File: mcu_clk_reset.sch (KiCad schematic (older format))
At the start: 52 parts, among them J4 20021121-00010C4LF, J5 M20-8762042, Q3 BSS214NW, Q4 BSS214NW, Q5 BSS214NW, Q6 BSS214NW, U4 IS25WP032D, U5 FE310-G002, X1 KX2132709Z, Y1 TSX-3225 16.0000MF18X-AC0

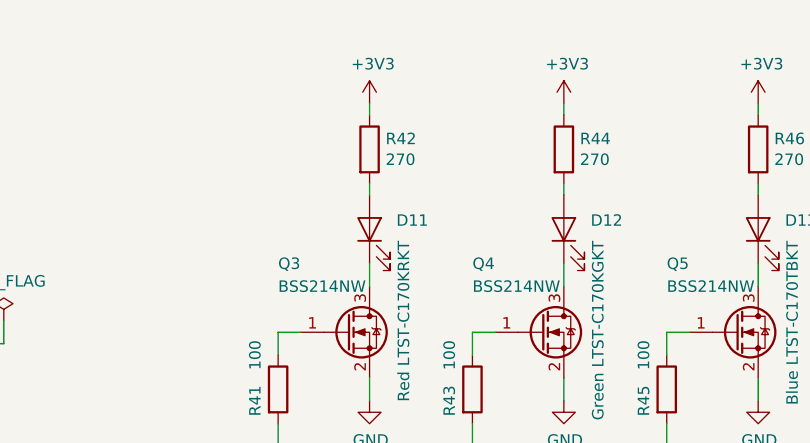
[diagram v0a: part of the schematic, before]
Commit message: Change resistor values to adjust LED brightness
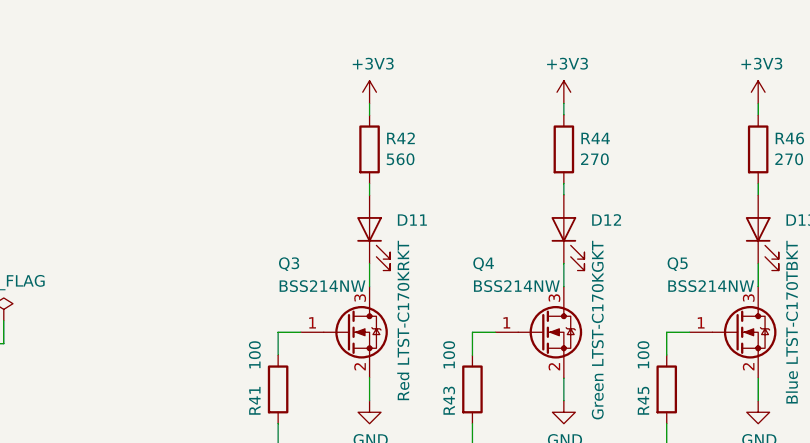
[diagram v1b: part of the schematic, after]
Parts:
- R42: value 270 -> 560
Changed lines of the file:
@@
 AR Path="/5E14DB51/5EBB9395" Ref="R42"  Part="1"
 F 0 "R42" H 8170 1196 50  0000 L CNN
-F 1 "270" H 8170 1105 50  0000 L CNN
+F 1 "560" H 8170 1105 50  0000 L CNN
 F 2 "Resistor_SMD:R_0603_1608Metric_Pad1.05x0.95mm_HandSolder" V 8030 1150 50  0001 C CNN
 F 3 "~" H 8100 1150 50  0001 C CNN

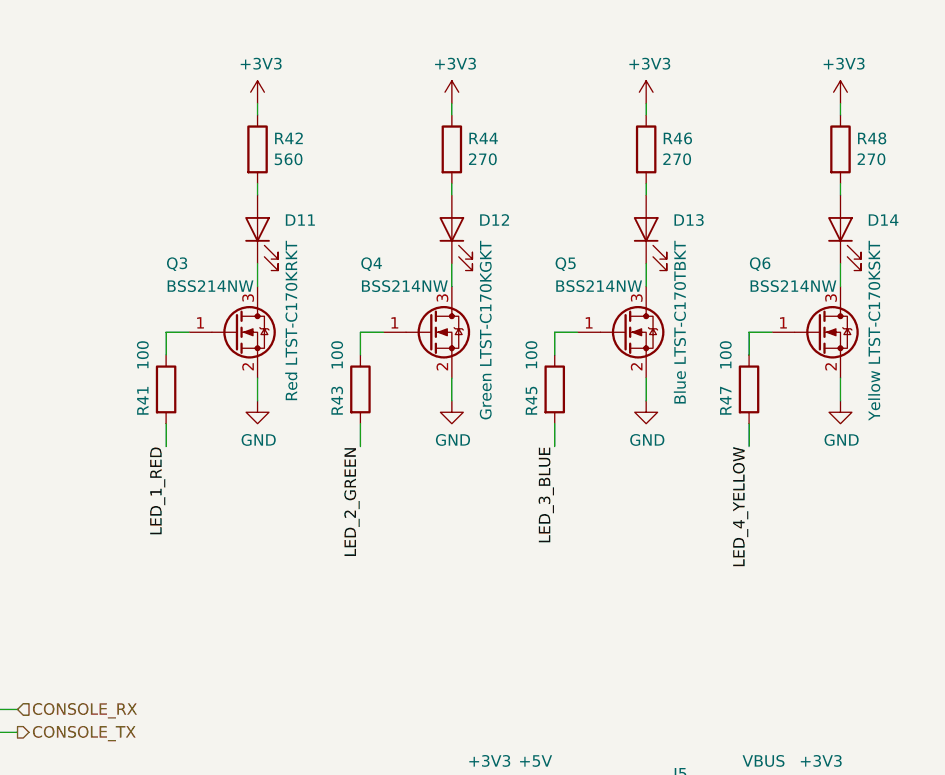
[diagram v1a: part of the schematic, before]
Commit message: Add 10k pull-downs on MCU LED outputs, improve layout
Pushed few traces, fixed DRC issue on one of the vias.
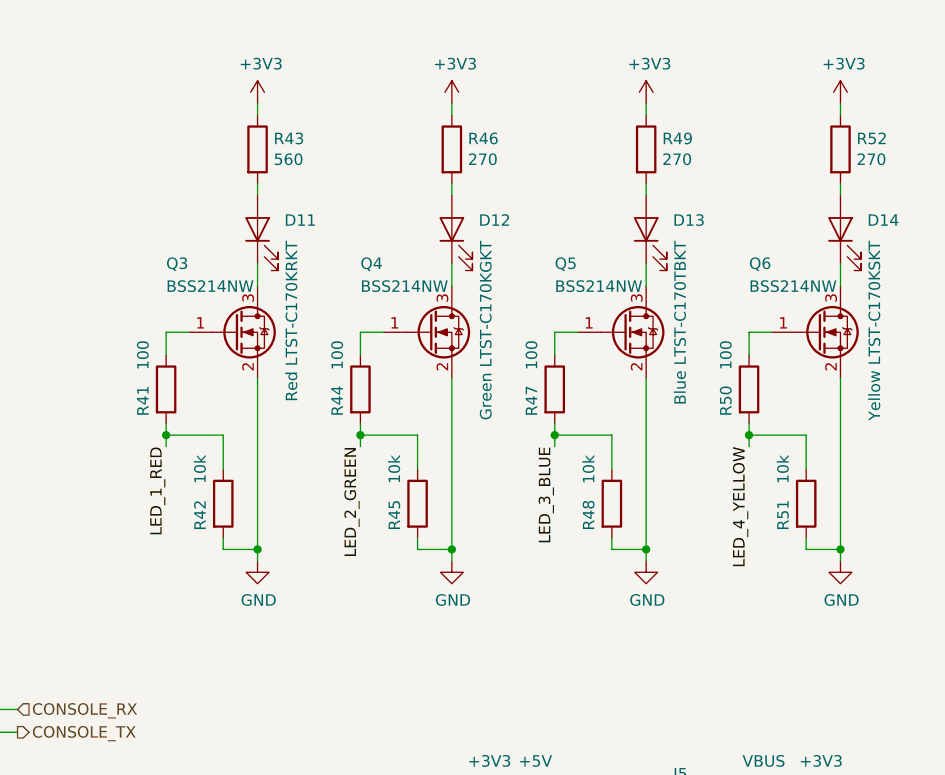
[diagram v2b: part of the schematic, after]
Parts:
- added R42, R45, R48, R51: 10k, Resistor_SMD:R_0603_1608Metric_Pad1.05x0.95mm_HandSolder, symbol Device:R
- renumbered R42 to R43, R43 to R44, R44 to R46, R45 to R47, R46 to R49, R47 to R50, R48 to R52
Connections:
- net GND: now also R42.2, R45.2, R48.2, R51.2
- net LED_1_RED: now also R42.1
- net LED_2_GREEN: now also R45.1
- net LED_3_BLUE: now also R48.1
- net LED_4_YELLOW: now also R51.1
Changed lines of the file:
@@
 L power:GND #PWR?
 U 1 1 5EB19EB2
-P 8950 2250
+P 8950 2950
 AR Path="/5E14D879/5EB19EB2" Ref="#PWR?"  Part="1"
 AR Path="/5E14DB51/5EB19EB2" Ref="#PWR048"  Part="1"
-F 0 "#PWR048" H 8950 2000 50  0001 C CNN
-F 1 "GND" H 8955 2077 50  0000 C CNN
-F 2 "" H 8950 2250 50  0001 C CNN
-F 3 "" H 8950 2250 50  0001 C CNN
-	1    8950 2250
+F 0 "#PWR048" H 8950 2700 50  0001 C CNN
+F 1 "GND" H 8955 2777 50  0000 C CNN
+F 2 "" H 8950 2950 50  0001 C CNN
+F 3 "" H 8950 2950 50  0001 C CNN
+	1    8950 2950
 	1    0    0    -1
 $EndComp
@@
 	1    0    0    -1
 $EndComp
-Wire Wire Line
-	8950 2150 8950 2250
 $Comp
 L power:+3V3 #PWR?
@@
 P 8950 1150
 AR Path="/5E14D879/5EB19ECC" Ref="R?"  Part="1"
-AR Path="/5E14DB51/5EB19ECC" Ref="R44"  Part="1"
-F 0 "R44" H 9020 1196 50  0000 L CNN
+AR Path="/5E14DB51/5EB19ECC" Ref="R46"  Part="1"
+F 0 "R46" H 9020 1196 50  0000 L CNN
 F 1 "270" H 9020 1105 50  0000 L CNN
 F 2 "Resistor_SMD:R_0603_1608Metric_Pad1.05x0.95mm_HandSolder" V 8880 1150 50  0001 C CNN
@@
 P 8550 2200
 AR Path="/5E14D879/5EB19ED2" Ref="R?"  Part="1"
-AR Path="/5E14DB51/5EB19ED2" Ref="R43"  Part="1"
-F 0 "R43" V 8450 2150 50  0000 C CNN
+AR Path="/5E14DB51/5EB19ED2" Ref="R44"  Part="1"
+F 0 "R44" V 8450 2150 50  0000 C CNN
 F 1 "100" V 8450 2350 50  0000 C CNN
 F 2 "Resistor_SMD:R_0603_1608Metric_Pad1.05x0.95mm_HandSolder" V 8480 2200 50  0001 C CNN
@@
 	8550 2050 8550 1950
 Wire Wire Line
-	8550 2450 8550 2350
+	8550 2450 8550 2400
 $Comp
 L Device:LED D?
@@
 L power:GND #PWR?
 U 1 1 5EBB9381
-P 8100 2250
+P 8100 2950
 AR Path="/5E14D879/5EBB9381" Ref="#PWR?"  Part="1"
 AR Path="/5E14DB51/5EBB9381" Ref="#PWR046"  Part="1"
-F 0 "#PWR046" H 8100 2000 50  0001 C CNN
-F 1 "GND" H 8105 2077 50  0000 C CNN
-F 2 "" H 8100 2250 50  0001 C CNN
-F 3 "" H 8100 2250 50  0001 C CNN
-	1    8100 2250
+F 0 "#PWR046" H 8100 2700 50  0001 C CNN
+F 1 "GND" H 8105 2777 50  0000 C CNN
+F 2 "" H 8100 2950 50  0001 C CNN
+F 3 "" H 8100 2950 50  0001 C CNN
+	1    8100 2950
 	1    0    0    -1
 $EndComp
@@
 	1    0    0    -1
 $EndComp
-Wire Wire Line
-	8100 2150 8100 2250
 $Comp
 L power:+3V3 #PWR?
@@
 P 8100 1150
 AR Path="/5E14D879/5EBB9395" Ref="R?"  Part="1"
-AR Path="/5E14DB51/5EBB9395" Ref="R42"  Part="1"
-F 0 "R42" H 8170 1196 50  0000 L CNN
+AR Path="/5E14DB51/5EBB9395" Ref="R43"  Part="1"
+F 0 "R43" H 8170 1196 50  0000 L CNN
 F 1 "560" H 8170 1105 50  0000 L CNN
 F 2 "Resistor_SMD:R_0603_1608Metric_Pad1.05x0.95mm_HandSolder" V 8030 1150 50  0001 C CNN
@@
 	7700 2050 7700 1950
 Wire Wire Line
-	7700 2450 7700 2350
+	7700 2450 7700 2400
 Wire Wire Line
 	8100 1650 8100 1750
@@
 L power:GND #PWR?
 U 1 1 5EC16F6B
-P 10650 2250
+P 10650 2950
 AR Path="/5E14D879/5EC16F6B" Ref="#PWR?"  Part="1"
 AR Path="/5E14DB51/5EC16F6B" Ref="#PWR057"  Part="1"
-F 0 "#PWR057" H 10650 2000 50  0001 C CNN
-F 1 "GND" H 10655 2077 50  0000 C CNN
-F 2 "" H 10650 2250 50  0001 C CNN
-F 3 "" H 10650 2250 50  0001 C CNN
-	1    10650 2250
+F 0 "#PWR057" H 10650 2700 50  0001 C CNN
+F 1 "GND" H 10655 2777 50  0000 C CNN
+F 2 "" H 10650 2950 50  0001 C CNN
+F 3 "" H 10650 2950 50  0001 C CNN
+	1    10650 2950
 	1    0    0    -1
 $EndComp
@@
 	1    0    0    -1
 $EndComp
-Wire Wire Line
-	10650 2150 10650 2250
 $Comp
 L power:+3V3 #PWR?
@@
 P 10650 1150
 AR Path="/5E14D879/5EC16F7F" Ref="R?"  Part="1"
-AR Path="/5E14DB51/5EC16F7F" Ref="R48"  Part="1"
-F 0 "R48" H 10720 1196 50  0000 L CNN
+AR Path="/5E14DB51/5EC16F7F" Ref="R52"  Part="1"
+F 0 "R52" H 10720 1196 50  0000 L CNN
 F 1 "270" H 10720 1105 50  0000 L CNN
 F 2 "Resistor_SMD:R_0603_1608Metric_Pad1.05x0.95mm_HandSolder" V 10580 1150 50  0001 C CNN
@@
 P 10250 2200
 AR Path="/5E14D879/5EC16F85" Ref="R?"  Part="1"
-AR Path="/5E14DB51/5EC16F85" Ref="R47"  Part="1"
-F 0 "R47" V 10150 2150 50  0000 C CNN
+AR Path="/5E14DB51/5EC16F85" Ref="R50"  Part="1"
+F 0 "R50" V 10150 2150 50  0000 C CNN
 F 1 "100" V 10150 2350 50  0000 C CNN
 F 2 "Resistor_SMD:R_0603_1608Metric_Pad1.05x0.95mm_HandSolder" V 10180 2200 50  0001 C CNN
@@
 	10250 2050 10250 1950
 Wire Wire Line
-	10250 2450 10250 2350
+	10250 2450 10250 2400
 Wire Wire Line
 	10650 1650 10650 1750
@@
 L power:GND #PWR?
 U 1 1 5EC16F97
-P 9800 2250
+P 9800 2950
 AR Path="/5E14D879/5EC16F97" Ref="#PWR?"  Part="1"
 AR Path="/5E14DB51/5EC16F97" Ref="#PWR052"  Part="1"
-F 0 "#PWR052" H 9800 2000 50  0001 C CNN
-F 1 "GND" H 9805 2077 50  0000 C CNN
-F 2 "" H 9800 2250 50  0001 C CNN
-F 3 "" H 9800 2250 50  0001 C CNN
-	1    9800 2250
+F 0 "#PWR052" H 9800 2700 50  0001 C CNN
+F 1 "GND" H 9805 2777 50  0000 C CNN
+F 2 "" H 9800 2950 50  0001 C CNN
+F 3 "" H 9800 2950 50  0001 C CNN
+	1    9800 2950
 	1    0    0    -1
 $EndComp
@@
 	1    0    0    -1
 $EndComp
-Wire Wire Line
-	9800 2150 9800 2250
 $Comp
 L power:+3V3 #PWR?
@@
 P 9800 1150
 AR Path="/5E14D879/5EC16FAB" Ref="R?"  Part="1"
-AR Path="/5E14DB51/5EC16FAB" Ref="R46"  Part="1"
-F 0 "R46" H 9870 1196 50  0000 L CNN
+AR Path="/5E14DB51/5EC16FAB" Ref="R49"  Part="1"
+F 0 "R49" H 9870 1196 50  0000 L CNN
 F 1 "270" H 9870 1105 50  0000 L CNN
 F 2 "Resistor_SMD:R_0603_1608Metric_Pad1.05x0.95mm_HandSolder" V 9730 1150 50  0001 C CNN
@@
 P 9400 2200
 AR Path="/5E14D879/5EC16FB1" Ref="R?"  Part="1"
-AR Path="/5E14DB51/5EC16FB1" Ref="R45"  Part="1"
-F 0 "R45" V 9300 2150 50  0000 C CNN
+AR Path="/5E14DB51/5EC16FB1" Ref="R47"  Part="1"
+F 0 "R47" V 9300 2150 50  0000 C CNN
 F 1 "100" V 9300 2350 50  0000 C CNN
 F 2 "Resistor_SMD:R_0603_1608Metric_Pad1.05x0.95mm_HandSolder" V 9330 2200 50  0001 C CNN
@@
 	9400 2050 9400 1950
 Wire Wire Line
-	9400 2450 9400 2350
+	9400 2450 9400 2400
 Wire Wire Line
 	9800 1650 9800 1750
@@
 	5600 3200 6100 3200
 $Comp
-L power:PWR_FLAG #FLG04
+L power:PWR_FLAG #FLG05
 U 1 1 5E39839C
 P 4950 1550
-F 0 "#FLG04" H 4950 1625 50  0001 C CNN
+F 0 "#FLG05" H 4950 1625 50  0001 C CNN
 F 1 "PWR_FLAG" H 4950 1723 50  0000 C CNN
 F 2 "" H 4950 1550 50  0001 C CNN
@@
 Connection ~ 4950 1600
 $Comp
-L power:PWR_FLAG #FLG05
+L power:PWR_FLAG #FLG06
 U 1 1 5E3B4680
 P 6500 1900
-F 0 "#FLG05" H 6500 1975 50  0001 C CNN
+F 0 "#FLG06" H 6500 1975 50  0001 C CNN
 F 1 "PWR_FLAG" H 6500 2073 50  0000 C CNN
 F 2 "" H 6500 1900 50  0001 C CNN
@@
 Text Label 3100 2500 2    50   ~ 0
 XTAL_N
+$Comp
+L Device:R R?
+U 1 1 5E95ECAB
+P 7950 2700
+AR Path="/5E14D879/5E95ECAB" Ref="R?"  Part="1"
+AR Path="/5E14DB51/5E95ECAB" Ref="R42"  Part="1"
+F 0 "R42" V 7850 2650 50  0000 C CNN
+F 1 "10k" V 7850 2850 50  0000 C CNN
+F 2 "Resistor_SMD:R_0603_1608Metric_Pad1.05x0.95mm_HandSolder" V 7880 2700 50  0001 C CNN
+F 3 "~" H 7950 2700 50  0001 C CNN
+	1    7950 2700
+	1    0    0    -1
+$EndComp
+$Comp
+L Device:R R?
+U 1 1 5E95F416
+P 8800 2700
+AR Path="/5E14D879/5E95F416" Ref="R?"  Part="1"
+AR Path="/5E14DB51/5E95F416" Ref="R45"  Part="1"
+F 0 "R45" V 8700 2650 50  0000 C CNN
+F 1 "10k" V 8700 2850 50  0000 C CNN
+F 2 "Resistor_SMD:R_0603_1608Metric_Pad1.05x0.95mm_HandSolder" V 8730 2700 50  0001 C CNN
+F 3 "~" H 8800 2700 50  0001 C CNN
+	1    8800 2700
+	1    0    0    -1
+$EndComp
+$Comp
+L Device:R R?
+U 1 1 5E95F72A
+P 9650 2700
+AR Path="/5E14D879/5E95F72A" Ref="R?"  Part="1"
+AR Path="/5E14DB51/5E95F72A" Ref="R48"  Part="1"
+F 0 "R48" V 9550 2650 50  0000 C CNN
+F 1 "10k" V 9550 2850 50  0000 C CNN
+F 2 "Resistor_SMD:R_0603_1608Metric_Pad1.05x0.95mm_HandSolder" V 9580 2700 50  0001 C CNN
+F 3 "~" H 9650 2700 50  0001 C CNN
+	1    9650 2700
+	1    0    0    -1
+$EndComp
+$Comp
+L Device:R R?
+U 1 1 5E95FA92
+P 10500 2700
+AR Path="/5E14D879/5E95FA92" Ref="R?"  Part="1"
+AR Path="/5E14DB51/5E95FA92" Ref="R51"  Part="1"
+F 0 "R51" V 10400 2650 50  0000 C CNN
+F 1 "10k" V 10400 2850 50  0000 C CNN
+F 2 "Resistor_SMD:R_0603_1608Metric_Pad1.05x0.95mm_HandSolder" V 10430 2700 50  0001 C CNN
+F 3 "~" H 10500 2700 50  0001 C CNN
+	1    10500 2700
+	1    0    0    -1
+$EndComp
+Wire Wire Line
+	10500 2550 10500 2400
+Wire Wire Line
+	10500 2400 10250 2400
+Connection ~ 10250 2400
+Wire Wire Line
+	10250 2400 10250 2350
+Wire Wire Line
+	9650 2550 9650 2400
+Wire Wire Line
+	9650 2400 9400 2400
+Connection ~ 9400 2400
+Wire Wire Line
+	9400 2400 9400 2350
+Wire Wire Line
+	8800 2550 8800 2400
+Wire Wire Line
+	8800 2400 8550 2400
+Connection ~ 8550 2400
+Wire Wire Line
+	8550 2400 8550 2350
+Wire Wire Line
+	7950 2550 7950 2400
+Wire Wire Line
+	7950 2400 7700 2400
+Connection ~ 7700 2400
+Wire Wire Line
+	7700 2400 7700 2350
+Wire Wire Line
+	9650 2850 9650 2900
+Wire Wire Line
+	9650 2900 9800 2900
+Wire Wire Line
+	9800 2150 9800 2900
+Wire Wire Line
+	9800 2950 9800 2900
+Connection ~ 9800 2900
+Wire Wire Line
+	8100 2150 8100 2900
+Wire Wire Line
+	7950 2850 7950 2900
+Wire Wire Line
+	7950 2900 8100 2900
+Connection ~ 8100 2900
+Wire Wire Line
+	8100 2900 8100 2950
+Wire Wire Line
+	10500 2850 10500 2900
+Wire Wire Line
+	10500 2900 10650 2900
+Wire Wire Line
+	10650 2900 10650 2950
+Wire Wire Line
+	10650 2150 10650 2900
+Connection ~ 10650 2900
+Wire Wire Line
+	8950 2150 8950 2900
+Wire Wire Line
+	8800 2850 8800 2900
+Wire Wire Line
+	8800 2900 8950 2900
+Connection ~ 8950 2900
+Wire Wire Line
+	8950 2900 8950 2950
 $EndSCHEMATC
